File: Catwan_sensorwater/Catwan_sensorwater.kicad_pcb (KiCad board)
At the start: 2 copper layers, 79.9 x 45 mm, 40 parts, among them J1 SENSOR 1, J10 VSP, J2 SENSOR 2, J3 SENSOR 3, J4 BATT, J5 USB_B, J6 Conn_01x04, J7 Conn_01x03, J8 Conn_01x03_Female, J9 SENSOR 4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

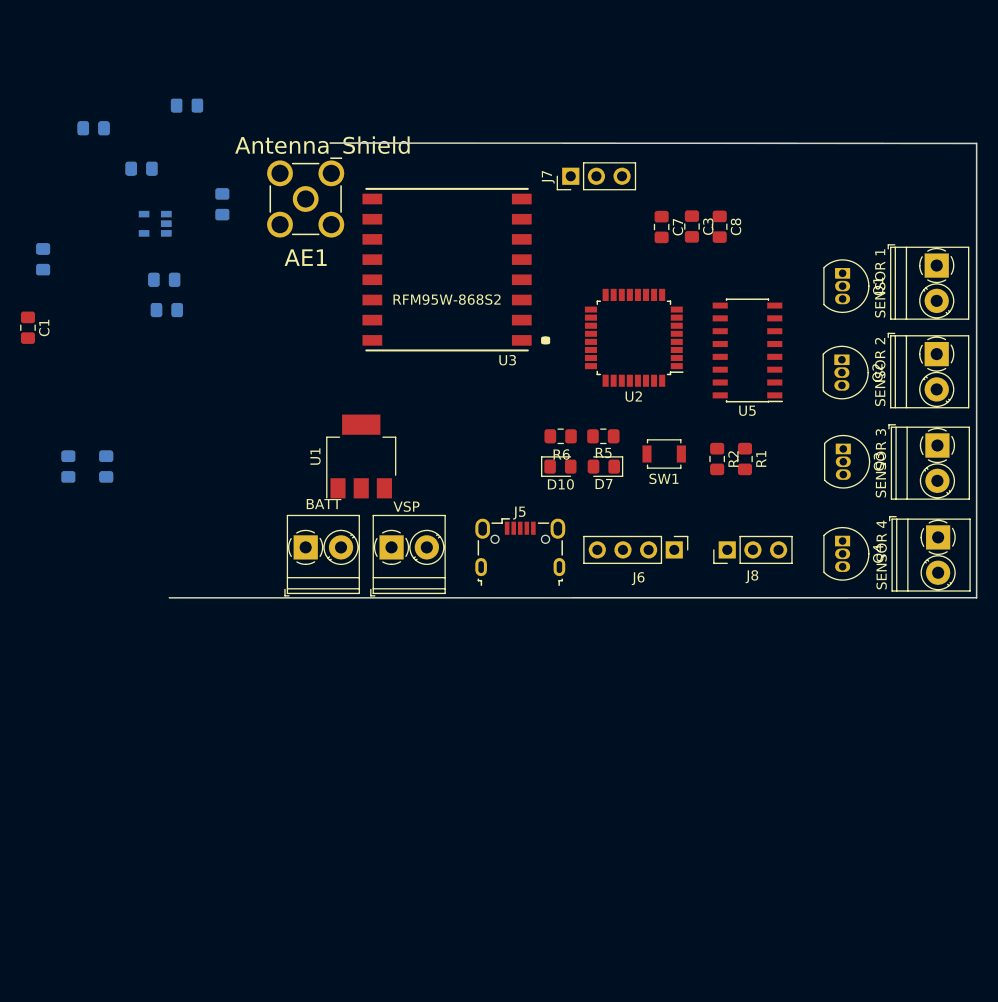
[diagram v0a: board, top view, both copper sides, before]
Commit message: components back to the front
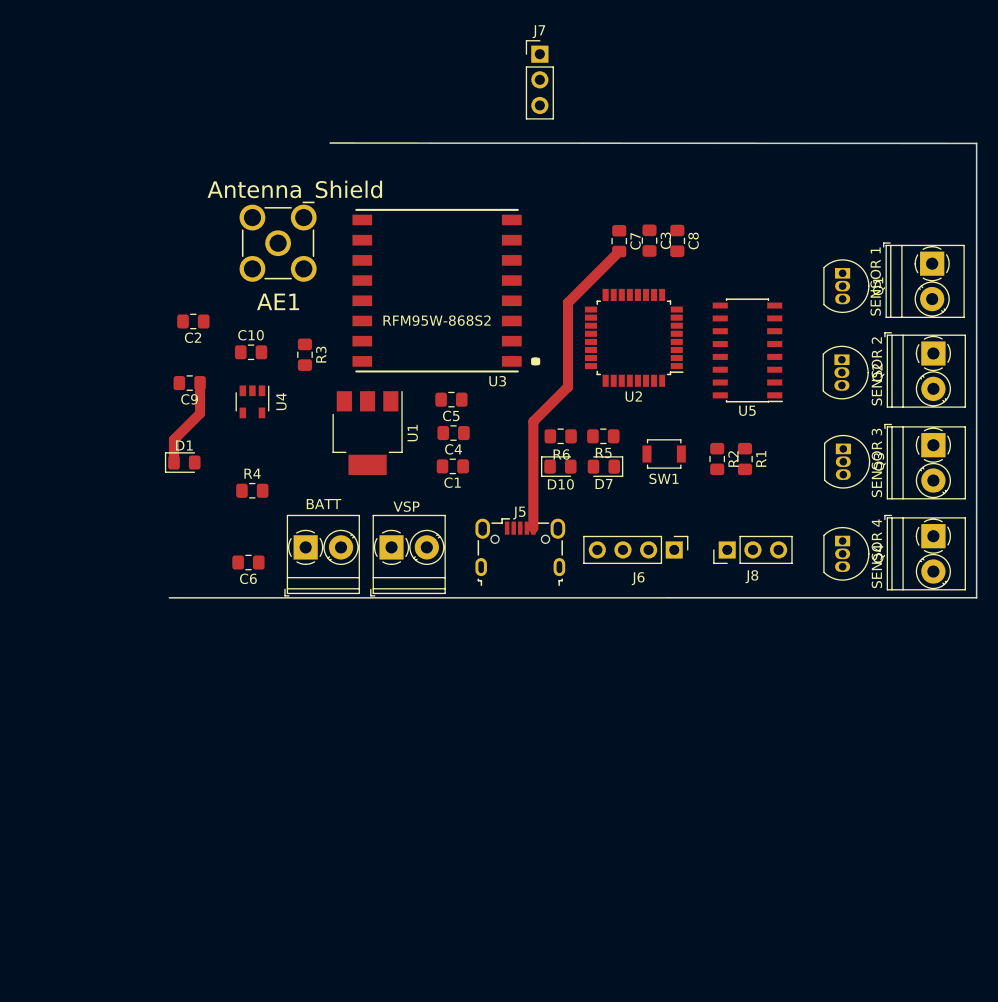
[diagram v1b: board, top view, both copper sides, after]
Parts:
- C10, C2, C4, C5, C6, C9, D1, R3, R4, U4: moved to F.Cu
- moved C6 45.7 mm to (108.3, 122.5), turned to 180 degrees
- moved C1 44.3 mm to (128.6, 113.0), turned to 180 degrees
- moved R4 39.2 mm to (108.7, 115.4)
- moved C4 38.3 mm to (128.6, 109.7), turned to 180 degrees
- moved C5 34.8 mm to (128.4, 106.4), turned to 180 degrees
- moved D1 25.9 mm to (102.0, 112.6), turned to 0 degrees
- moved R3 24.5 mm to (113.9, 101.9), turned to 270 degrees
- moved U4 20.1 mm to (108.7, 106.6), turned to 270 degrees
- moved C2 16.1 mm to (102.9, 98.6), turned to 180 degrees
- moved J7 12.5 mm to (137.2, 72.2), turned to 0 degrees
- moved C10 11.2 mm to (108.6, 101.7)
- moved C9 7.58 mm to (102.5, 104.7), turned to 180 degrees
- moved AE1 5.16 mm to (111.3, 90.9)
- moved C3 4.43 mm to (148.1, 90.6)
- moved C8 4.43 mm to (150.8, 90.7)
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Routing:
- net GND: track 0.00 -> 30.9 mm
- net VCC: track 0.00 -> 8.94 mm

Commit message: diode shottkie and regulator packege
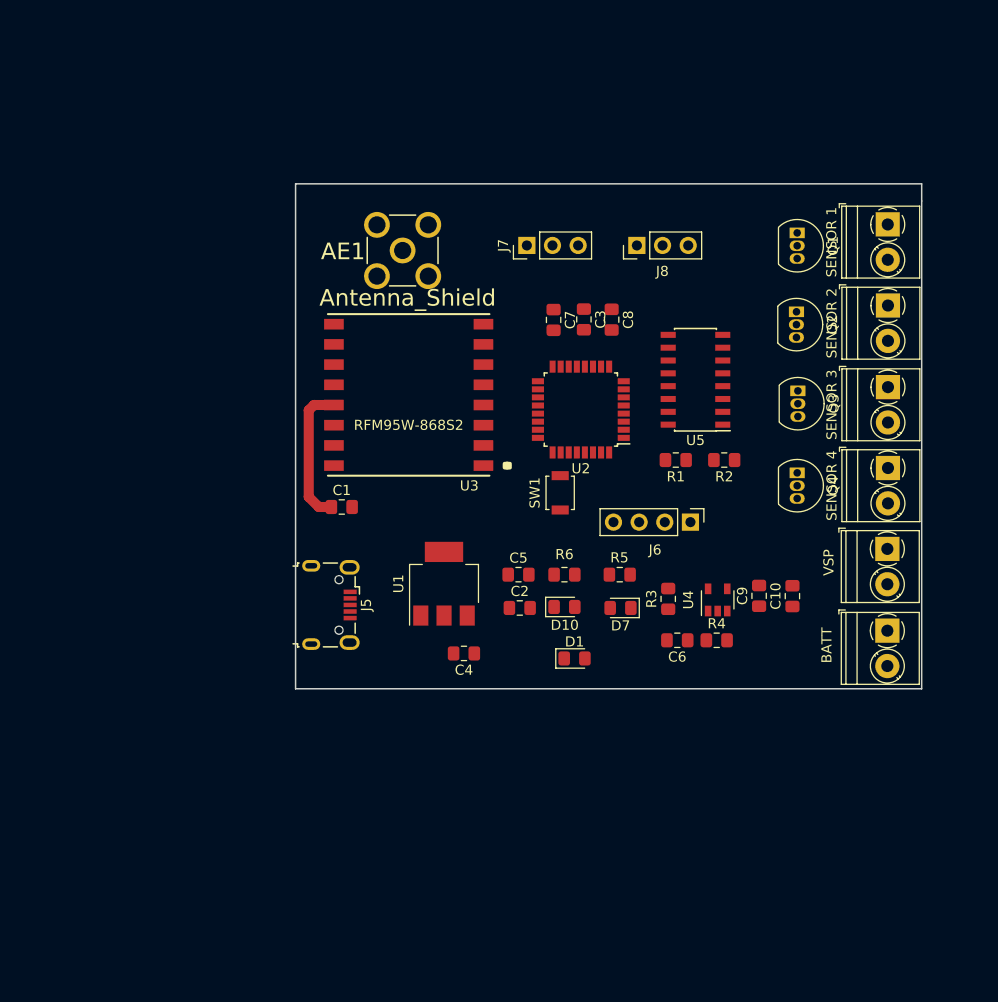
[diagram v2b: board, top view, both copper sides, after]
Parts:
- moved C9 60.2 mm to (158.9, 125.8), turned to 90 degrees
- moved C10 58.8 mm to (162.2, 125.8), turned to 90 degrees
- moved J4 58.2 mm to (171.6, 129.2), turned to 270 degrees
- moved U4 50.1 mm to (154.8, 126.2), turned to 90 degrees
- moved J10 49.1 mm to (171.6, 121.2), turned to 270 degrees
- moved R4 48.3 mm to (154.7, 130.2)
- moved R3 43.3 mm to (149.9, 126.1), turned to 90 degrees
- moved D1 43.2 mm to (140.6, 132.0)
- moved C6 43.2 mm to (150.8, 130.2)
- moved C2 43.0 mm to (135.2, 127.0), turned to 0 degrees
- moved J8 31.5 mm to (146.8, 91.1)
- moved C4 21.8 mm to (129.7, 131.5)
- moved J5 19.6 mm to (116.5, 126.7), turned to 270 degrees
- moved J7 19.0 mm to (135.9, 91.1), turned to 90 degrees
- moved C5 18.6 mm to (135.1, 123.7), turned to 0 degrees
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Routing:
- net GND: track 30.9 -> 0.00 mm
- net +3V3: track 0.00 -> 14.0 mm
- net VCC: track 8.94 -> 0.00 mm
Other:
- board size 79.9 x 45 mm -> 62 x 50 mm
- net class SOURCE: trace_width 1 -> 0.5

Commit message: new accommodation
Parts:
- U1: footprint Package_TO_SOT_SMD:SOT-223 -> Package_TO_SOT_SMD:SOT-223-3_TabPin2
- moved J4 54.2 mm to (127.6, 160.8), turned to 180 degrees
- moved J10 53.5 mm to (135.8, 160.8), turned to 180 degrees
- moved R6 34.6 mm to (163.0, 149.2), turned to 180 degrees
- moved J5 32.5 mm to (116.8, 159.2), turned to 0 degrees
- moved C10 30.4 mm to (140.4, 147.1), turned to 270 degrees
- moved D10 30.2 mm to (163.0, 146.0), turned to 180 degrees
- moved R5 28.4 mm to (157.5, 149.2), turned to 0 degrees
- moved C9 26.2 mm to (143.7, 147.1), turned to 270 degrees
- moved D1 25.2 mm to (145.5, 156.7), turned to 180 degrees
- moved D7 22.6 mm to (157.4, 145.9), turned to 0 degrees
- moved U4 21.7 mm to (147.8, 146.7), turned to 270 degrees
- moved C5 21.6 mm to (127.0, 143.7), turned to 270 degrees
- moved R3 21.5 mm to (152.4, 147.5), turned to 270 degrees
- moved U1 19.2 mm to (120.6, 142.4), turned to 180 degrees
- moved C4 18.5 mm to (123.4, 148.9), turned to 0 degrees
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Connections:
- C4 pad 1: Net-(C4-Pad1) -> VCC

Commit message: Corrections
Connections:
- C6 pad 2: /BAT -> Net-(C6-Pad2)
- D1 pad 2: /BAT -> GND
- J10 pad 2: /Vsp -> VCC
- J4 pad 1: /BAT -> GND
- R4 pad 2: /BAT -> Net-(C6-Pad2)

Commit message: source
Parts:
- moved U1 44.4 mm to (160.5, 122.9), turned to 0 degrees
- moved J5 44.0 mm to (119.3, 115.3), turned to 270 degrees
- moved C5 41.4 mm to (157.4, 115.6)
- moved C2 41.4 mm to (160.5, 115.5)
- moved J4 37.2 mm to (137.0, 124.8)
- moved J10 36.7 mm to (129.0, 124.8)
- moved R5 34.3 mm to (147.2, 116.5)
- moved C9 33.5 mm to (128.9, 117.0), turned to 90 degrees
- moved R6 33.3 mm to (147.2, 120.0)
- moved D1 33.1 mm to (142.9, 123.7)
- moved R3 32.4 mm to (142.8, 116.5), turned to 180 degrees
- moved C4 32.0 mm to (126.1, 117.0), turned to 90 degrees
- moved U4 31.6 mm to (137.1, 117.0)
- moved C1 31.5 mm to (137.3, 92.4), turned to 90 degrees
- moved C10 31.1 mm to (132.3, 117.0), turned to 90 degrees
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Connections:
- C6 pad 2: Net-(C6-Pad2) -> /BAT
- D1 pad 2: GND -> /BAT
- J4 pad 1: GND -> /BAT
- R4 pad 2: Net-(C6-Pad2) -> /BAT
- U2 pad 3: /SENS_X -> /SENS_Y
- U2 pad 6: /SENS_Y -> /SENS_X
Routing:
- net VCC: track 0.00 -> 76.9 mm, vias 0 -> 5
- net +3V3: track 14.0 -> 69.2 mm, vias 0 -> 2
- net /D-: track 0.00 -> 27.5 mm
- net /D+: track 0.00 -> 27.4 mm
- net GND: track 0.00 -> 19.8 mm, vias 0 -> 1
- net /SENS_Y: track 0.00 -> 18.7 mm
- net /BAT: track 0.00 -> 12.2 mm
- net Net-(R4-Pad1): track 0.00 -> 11.4 mm, vias 0 -> 2
- net Net-(R5-Pad1): track 0.00 -> 11.3 mm
- net /SENS_X: track 0.00 -> 8.22 mm
- net /S1: track 0.00 -> 7.98 mm
- net /S0: track 0.00 -> 7.79 mm
- net Net-(R3-Pad2): track 0.00 -> 4.47 mm
- net Net-(D7-Pad1): track 0.00 -> 2.35 mm
- net Net-(D10-Pad1): track 0.00 -> 2.34 mm
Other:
- board size 62 x 50 mm -> 65 x 50 mm

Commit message: Rooteo new accommodation
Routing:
- net /DIO1: track 0.00 -> 39.9 mm
- net Net-(J2-Pad1): track 0.00 -> 31.8 mm
- net Net-(J1-Pad2): track 0.00 -> 29.2 mm
- net Net-(J9-Pad1): track 0.00 -> 27.7 mm
- net Net-(J1-Pad1): track 0.00 -> 27.4 mm
- net +3V3: track 69.2 -> 94.2 mm
- net Net-(J3-Pad1): track 0.00 -> 16.8 mm
- net Net-(J9-Pad2): track 0.00 -> 15.6 mm
- net Net-(AE1-Pad1): track 0.00 -> 14.3 mm
- net GND: track 19.8 -> 33.5 mm
- net Net-(J3-Pad2): track 0.00 -> 12.8 mm
- net /MOSI: track 0.00 -> 12.5 mm
- net Net-(J2-Pad2): track 0.00 -> 11.7 mm
- net /SWDIO: track 0.00 -> 9.82 mm
- net /Tx: track 0.00 -> 9.78 mm
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
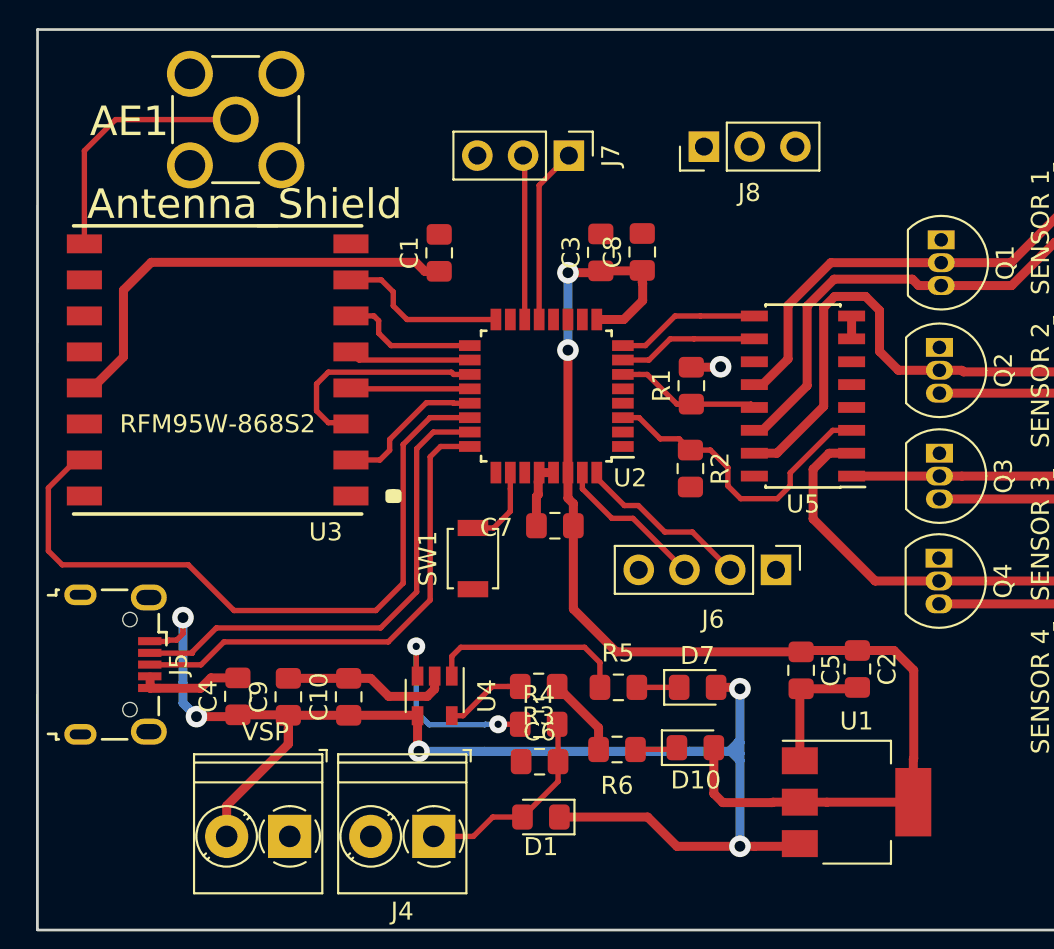
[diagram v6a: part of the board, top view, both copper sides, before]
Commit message: Rooteo GND
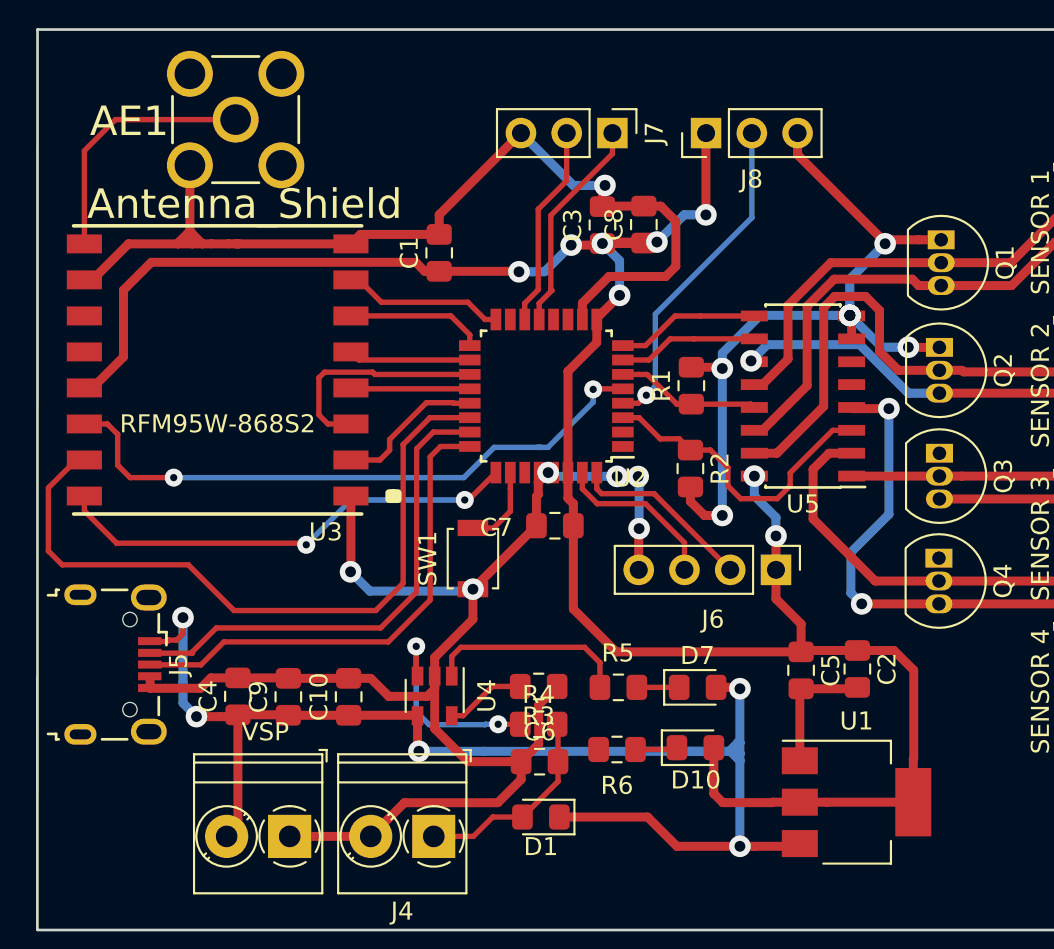
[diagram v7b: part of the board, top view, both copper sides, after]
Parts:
- moved J7 2.72 mm to (146.9, 85.8)
- moved C3 1.52 mm to (146.4, 90.9)
- moved C8 1.52 mm to (148.7, 90.8)
- moved J8 0.76 mm to (152.1, 85.8)
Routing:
- net GND: track 33.5 -> 190.4 mm, vias 1 -> 15
- net /DIO0: track 0.00 -> 35.2 mm, vias 0 -> 2
- net +3V3: track 94.2 -> 122.8 mm, vias 2 -> 8
- net /DIO2: track 0.00 -> 26.1 mm, vias 0 -> 2
- net /DHT_DAT: track 0.00 -> 18.5 mm, vias 0 -> 1
- net Net-(J9-Pad2): track 15.6 -> 33.9 mm, vias 0 -> 2
- net Net-(J2-Pad2): track 11.7 -> 23.9 mm, vias 0 -> 1
- net /Tx: track 9.78 -> 12.1 mm
- net /Rx: track 9.14 -> 11.3 mm
- net VCC: track 76.9 -> 75.0 mm
- net /SWCLK: track 8.43 -> 9.32 mm

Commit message: Changes rooteo
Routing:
- net /DIO0: track 35.2 -> 0.49 mm, vias 2 -> 0
- net GND: track 190.4 -> 164.9 mm, vias 15 -> 11
- net /EN: track 0.00 -> 23.6 mm, vias 0 -> 4
- net Net-(J2-Pad2): track 23.9 -> 11.7 mm, vias 1 -> 0
- net +3V3: track 122.8 -> 123.5 mm, vias 8 -> 6
